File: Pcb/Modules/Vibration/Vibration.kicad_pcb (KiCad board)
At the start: 2 copper layers, 50.8 x 20.3 mm, 11 parts, among them J1 JACK_RJ45, P1 C+, P2 C-, X1 HOLE, X2 HOLE, X3 HOLE, X4 HOLE, X5 HOLE, X6 HOLE

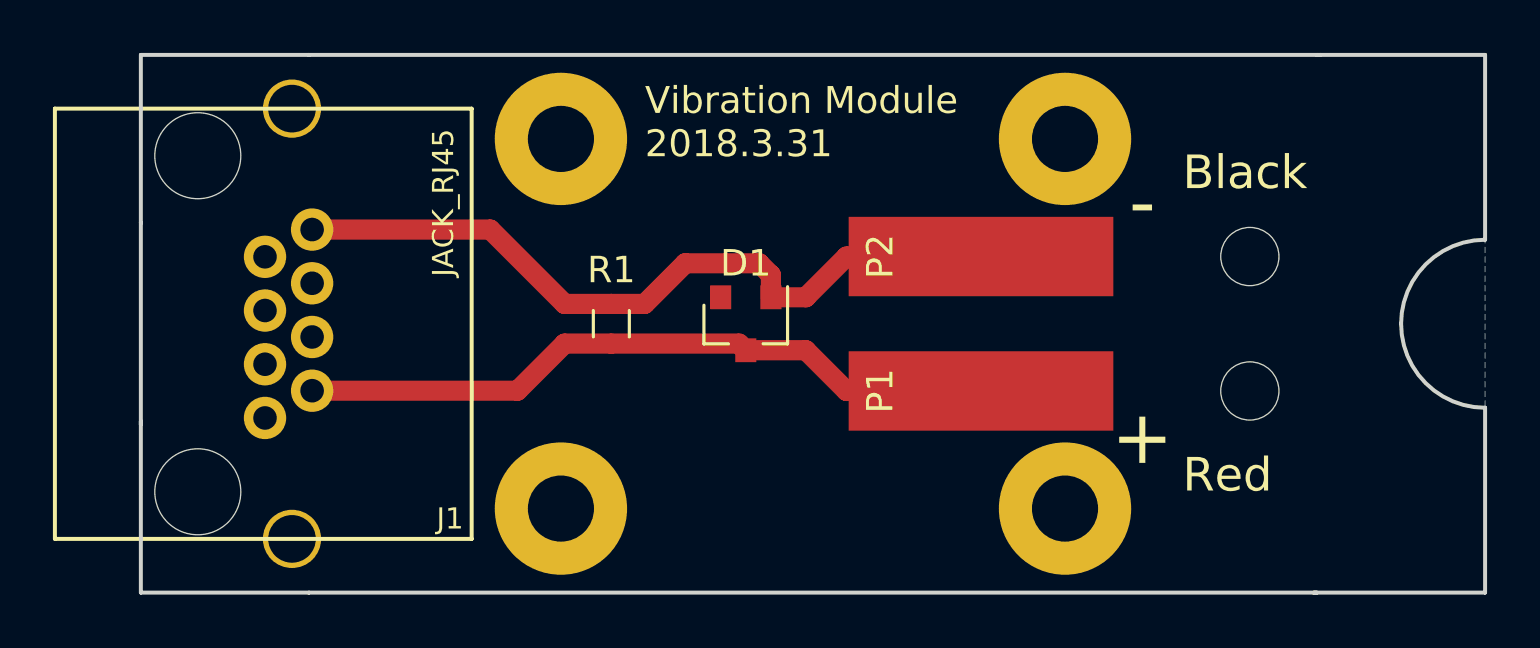
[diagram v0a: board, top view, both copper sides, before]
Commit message: Update module pcbs to fix minor issues and round corners
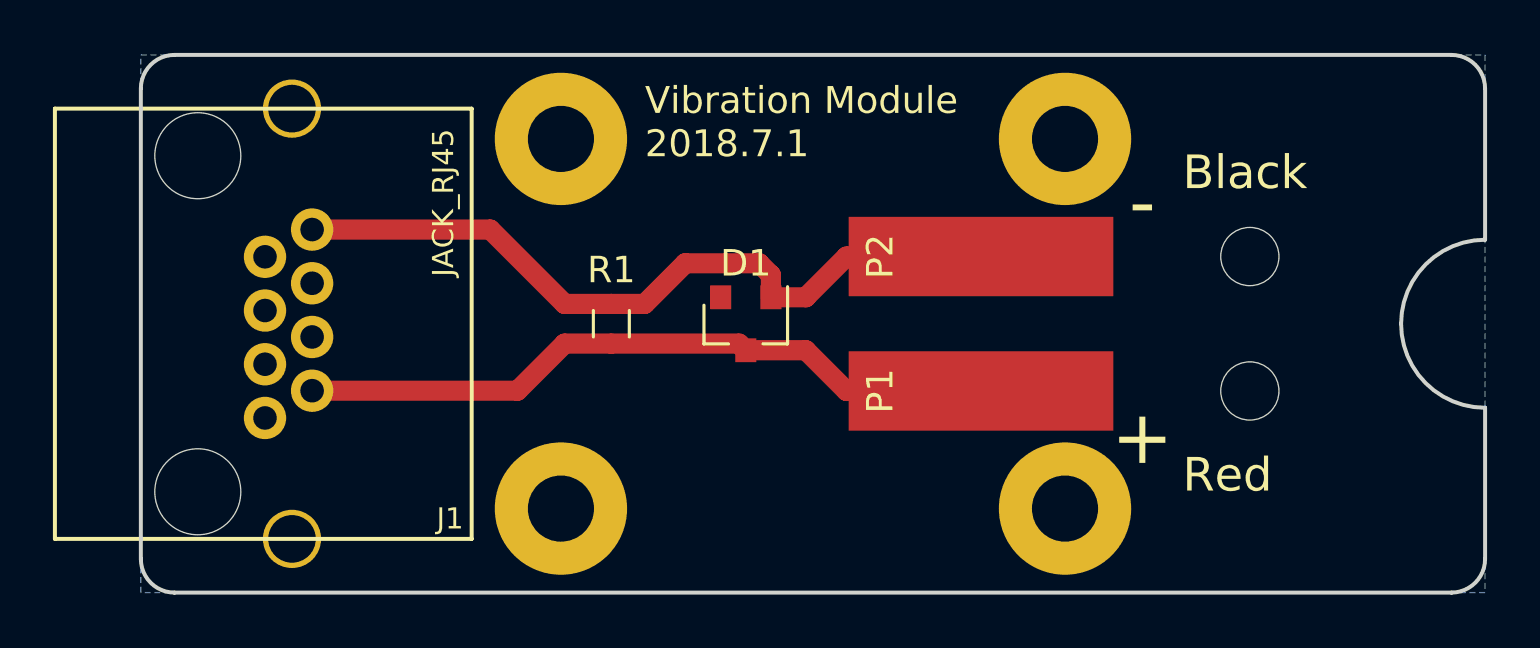
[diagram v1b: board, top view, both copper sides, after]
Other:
- outline, holes or cut-outs redrawn
- board text added: "Vibration Module 2018.7.1"
- board text removed: "Vibration Module 2018.3.31"
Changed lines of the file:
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@@
     (area 21.873869 24.0968 76.275001 47.1232)
     (thickness 1.6)
-    (drawings 19)
+    (drawings 16)
     (tracks 21)
     (zones 0)
@@
     (pad 1 thru_hole circle (at 0 0) (size 5 5) (drill 2.5) (layers *.Cu *.Mask))
   )
-  (gr_line (start 76.2 32.385) (end 76.2 25.4) (angle 90) (layer Edge.Cuts) (width 0.15))
-  (gr_line (start 76.2 45.72) (end 76.2 38.735) (angle 90) (layer Edge.Cuts) (width 0.15))
+  (gr_line (start 74.93 25.4) (end 26.67 25.4) (angle 90) (layer Edge.Cuts) (width 0.15))
+  (gr_line (start 76.2 32.385) (end 76.2 26.67) (angle 90) (layer Edge.Cuts) (width 0.15))
+  (gr_line (start 76.2 38.735) (end 76.2 44.45) (angle 90) (layer Edge.Cuts) (width 0.15))
+  (gr_line (start 74.93 45.72) (end 26.67 45.72) (angle 90) (layer Edge.Cuts) (width 0.15))
+  (gr_line (start 25.4 26.67) (end 25.4 44.45) (angle 90) (layer Edge.Cuts) (width 0.15))
+  (gr_arc (start 74.93 26.67) (end 74.93 25.4) (angle 90) (layer Edge.Cuts) (width 0.15))
+  (gr_arc (start 74.93 44.45) (end 76.2 44.45) (angle 90) (layer Edge.Cuts) (width 0.15))
+  (gr_arc (start 26.67 44.45) (end 26.67 45.72) (angle 90) (layer Edge.Cuts) (width 0.15))
+  (gr_arc (start 26.67 26.67) (end 25.4 26.67) (angle 90) (layer Edge.Cuts) (width 0.15))
   (gr_arc (start 76.2 35.56) (end 76.2 38.735) (angle 90) (layer Edge.Cuts) (width 0.15))
   (gr_arc (start 76.2 35.56) (end 73.025 35.56) (angle 90) (layer Edge.Cuts) (width 0.15))
@@
     (effects (font (size 1.27 1.27) (thickness 0.254)) (justify left))
   )
-  (gr_line (start 25.4 25.4) (end 31.75 25.4) (angle 90) (layer Edge.Cuts) (width 0.15))
-  (gr_line (start 25.4 31.75) (end 25.4 25.4) (angle 90) (layer Edge.Cuts) (width 0.15))
-  (gr_line (start 25.4 45.72) (end 25.4 39.243) (angle 90) (layer Edge.Cuts) (width 0.15))
-  (gr_line (start 31.75 45.72) (end 25.4 45.72) (angle 90) (layer Edge.Cuts) (width 0.15))
-  (gr_line (start 69.977 25.4) (end 69.85 25.4) (angle 90) (layer Edge.Cuts) (width 0.15))
-  (gr_line (start 69.977 25.4) (end 76.2 25.4) (angle 90) (layer Edge.Cuts) (width 0.15))
-  (gr_line (start 69.723 45.72) (end 76.2 45.72) (angle 90) (layer Edge.Cuts) (width 0.15))
   (gr_text + (at 63.246 39.878) (layer F.SilkS)
     (effects (font (size 2.032 2.032) (thickness 0.3)))
@@
     (effects (font (size 2.032 2.032) (thickness 0.3)))
   )
-  (gr_line (start 25.4 31.75) (end 25.4 39.37) (angle 90) (layer Edge.Cuts) (width 0.15))
-  (gr_text "Vibration Module\n2018.3.31" (at 44.45 27.94) (layer F.SilkS)
+  (gr_text "Vibration Module\n2018.7.1" (at 44.45 27.94) (layer F.SilkS)
     (effects (font (size 1.016 1.016) (thickness 0.2032)) (justify left))
   )
-  (gr_line (start 69.85 45.72) (end 31.75 45.72) (angle 90) (layer Edge.Cuts) (width 0.15))
-  (gr_line (start 31.75 25.4) (end 69.85 25.4) (angle 90) (layer Edge.Cuts) (width 0.15))
   (segment (start 31.872 32) (end 38.604 32) (width 0.762) (layer F.Cu) (net 1))
   (segment (start 41.414 34.81) (end 43.18 34.81) (width 0.762) (layer F.Cu) (net 1))
